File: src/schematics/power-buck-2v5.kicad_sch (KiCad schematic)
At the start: 9 parts, among them U4 TPS562202DRLR

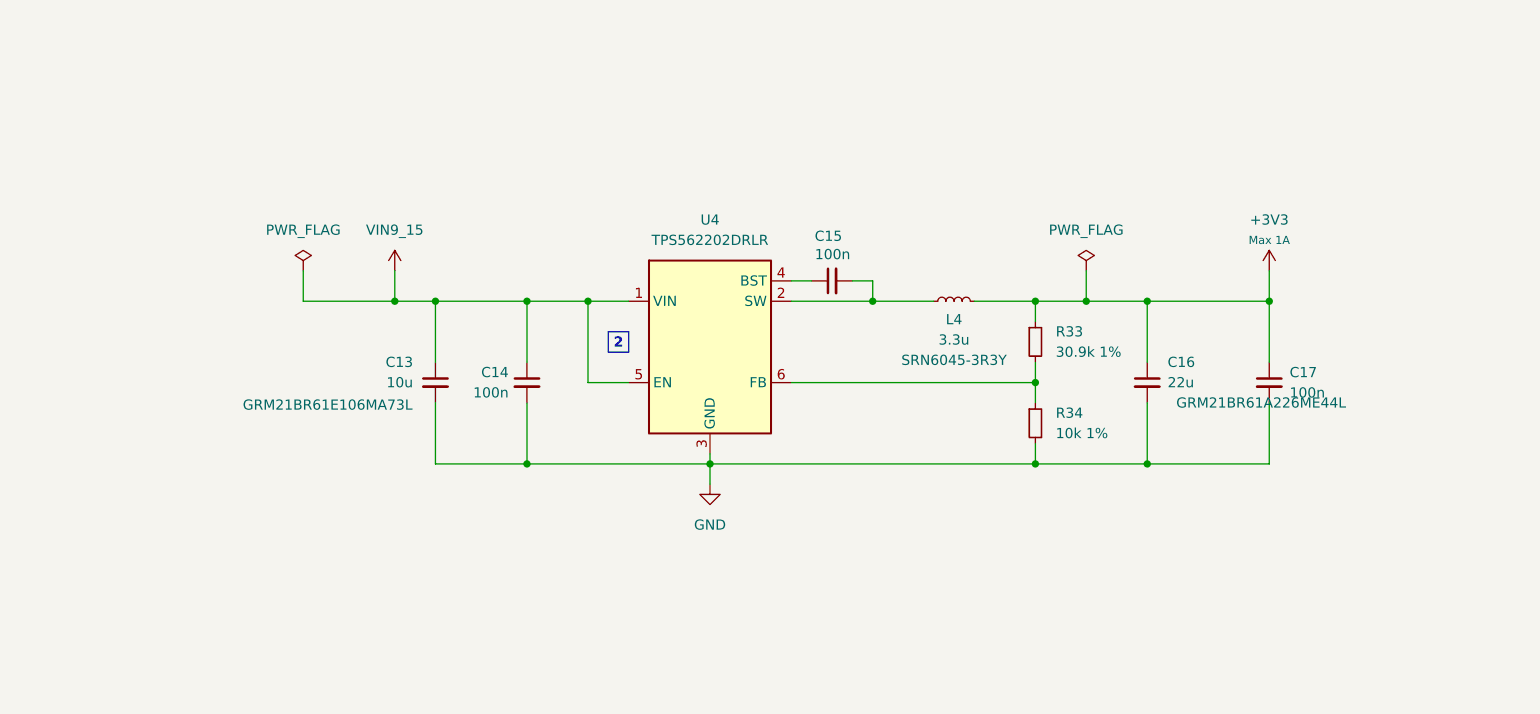
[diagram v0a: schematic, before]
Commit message: Fix schematic issues
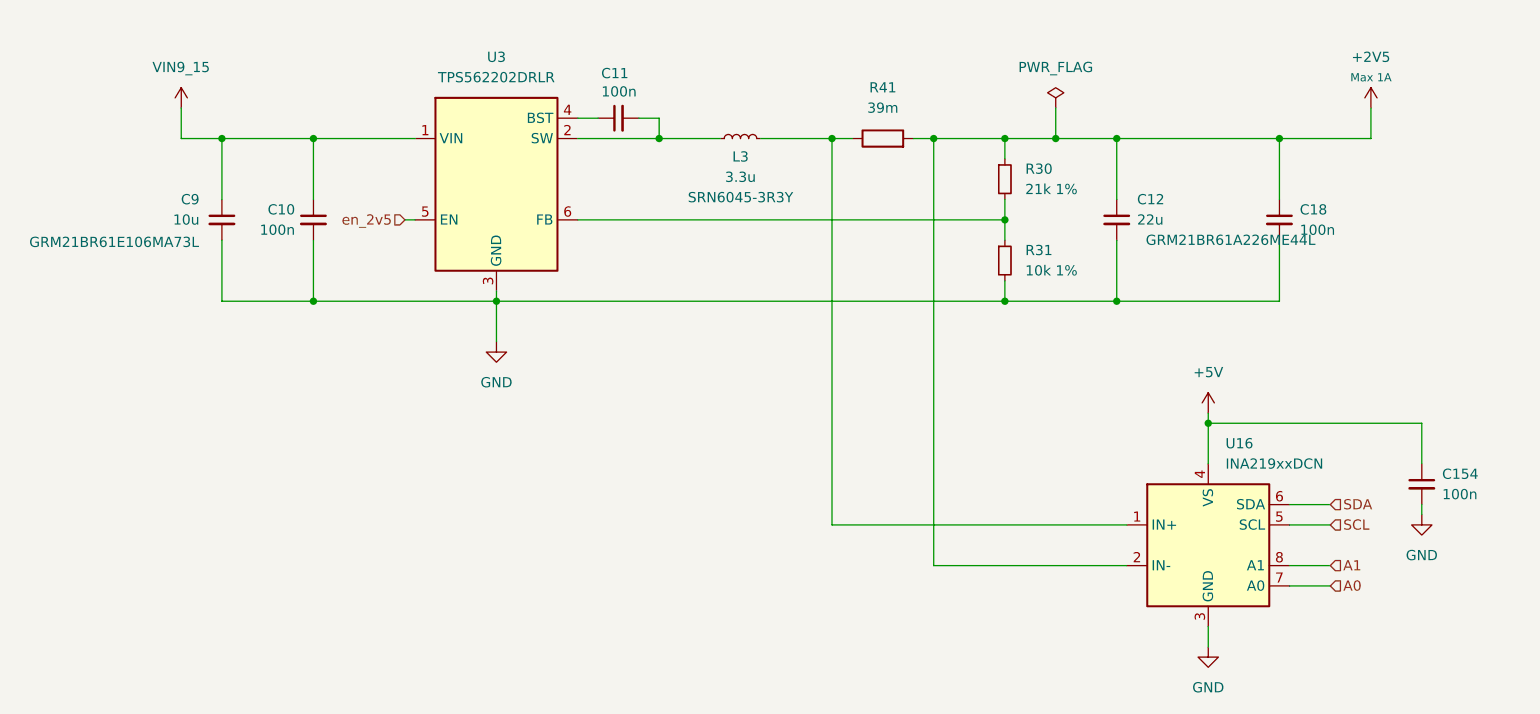
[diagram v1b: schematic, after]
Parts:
- removed C13: 10u, Capacitor_SMD:C_0805_2012Metric, symbol Device:C_Small
- removed C14, C17: 100n, Capacitor_SMD:C_0805_2012Metric, symbol Device:C_Small
- removed C15: 100n, Capacitor_SMD:C_0402_1005Metric, symbol Device:C_Small
- removed C16: 22u, Capacitor_SMD:C_0805_2012Metric, symbol Device:C_Small
- removed L4: 3.3u, ECAP5-DPROC:Coilcraft_XAL4030, symbol Device:L_Small
- removed R33: 30.9k 1%, Resistor_SMD:R_0402_1005Metric, symbol Device:R_Small
- removed R34: 10k 1%, Resistor_SMD:R_0402_1005Metric, symbol Device:R_Small
- removed U4: TPS562202DRLR, ECAP5-DPROC:TI_DRL0006A, symbol ECAP5-BSOM:TPS562202DRLR
- added C10, C18: 100n, Capacitor_SMD:C_0805_2012Metric, symbol Device:C_Small
- added C11, C154: 100n, Capacitor_SMD:C_0402_1005Metric, symbol Device:C_Small
- added C12: 22u, Capacitor_SMD:C_0805_2012Metric, symbol Device:C_Small
- added C9: 10u, Capacitor_SMD:C_0805_2012Metric, symbol Device:C_Small
- added L3: 3.3u, ECAP5-DPROC:Coilcraft_XAL4030, symbol Device:L_Small
- added R30: 21k 1%, Resistor_SMD:R_0402_1005Metric, symbol Device:R_Small
- added R31: 10k 1%, Resistor_SMD:R_0402_1005Metric, symbol Device:R_Small
- added R41: 39m, Resistor_SMD:R_1206_3216Metric, symbol Device:R
- added U16: INA219xxDCN, Package_TO_SOT_SMD:SOT-23-8, symbol ECAP5-BSOM:INA219xxDCN
- added U3: TPS562202DRLR, ECAP5-DPROC:TI_DRL0006A, symbol ECAP5-BSOM:TPS562202DRLR
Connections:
- net GND: now also C10.2, C12.2, C154.2, C18.2, C9.2, R31.2, U16.3 (GND), U3.3 (GND)
- net VIN9_15: now also C10.1, C9.1, U3.1 (VIN)
- new net: L3.2, R41.1, U16.1 (IN+)
- new net: R30.2, R31.1, U3.6 (FB)
- new net: C11.2, L3.1, U3.2 (SW)
- new net: C11.1, U3.4 (BST)
- new net +2V5: C12.1, C18.1, R30.1, R41.2, U16.2 (IN-)
- new net +5V: C154.1, U16.4 (VS)
- new net A0: U16.7 (A0)
- new net A1: U16.8 (A1)
- new net SCL: U16.5 (SCL)
- new net SDA: U16.6 (SDA)
- new net en_2v5: U3.5 (EN)

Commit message: Add bom components
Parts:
- C10, C18: MPN (none) -> SH21B104K101CT; Manufacturer (none) -> Walsin; Mouting Technology (none) -> SMD
- C11, C154: MPN (none) -> C1005X7R1C104M050BC; Manufacturer (none) -> TDK; Mouting Technology (none) -> SMD
- C12: MPN (none) -> GRM21BR61A226ME44L; Manufacturer (none) -> Murata Electronics; Mouting Technology (none) -> SMD; Part GRM21BR61A226ME44L -> (none)
- C9: MPN (none) -> GRM21BR61E106MA73L; Manufacturer (none) -> Murata Electronics; Mouting Technology (none) -> SMD; Part GRM21BR61E106MA73L -> (none)
- L3: MPN (none) -> SRN6045-3R3Y; Manufacturer (none) -> Bourns; Mouting Technology (none) -> SMD; Part SRN6045-3R3Y -> (none)
- R30: MPN (none) -> AC0402FR-0721KL; Manufacturer (none) -> YAGEO; Mouting Technology (none) -> SMD
- R31: MPN (none) -> CRCW040210K0FKEDC; Manufacturer (none) -> Vishay; Mouting Technology (none) -> SMD
- R41: MPN (none) -> PE1206FRE470R039L; Manufacturer (none) -> YAGEO; Mouting Technology (none) -> SMD
- U16: MPN (none) -> INA219AIDCNR; Manufacturer (none) -> Texas Instruments; Mouting Technology (none) -> SMD
- U3: MPN (none) -> TPS562202DRLR; Manufacturer (none) -> Texas Instruments; Mouting Technology (none) -> SMD
